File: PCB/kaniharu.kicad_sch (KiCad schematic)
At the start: 0 parts

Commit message: Remove autosave and lock files, add backup ZIP
Deleted KiCad autosave and lock files from the PCB directory and added a new backup ZIP file. Updated the main schematic file, likely reflecting recent design changes or cleanup.
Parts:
- added C10, C8, C9: C, symbol Device:C
- added C6, C7: 8p, symbol Device:C
- added J1: RJ45_Bel_SI-60062-F, Connector_RJ:RJ45_Bel_SI-60062-F, symbol Connector:RJ45_Bel_SI-60062-F
- added R5: 1.5k, symbol Device:R
- added R6, R7: 2.2k, symbol Device:R
- added R8: R, symbol Device:R
- added U1: STM32H743ZITx, Package_QFP:LQFP-144_20x20mm_P0.5mm, symbol MCU_ST_STM32H7:STM32H743ZITx
- added U3: DP83822IRHBR, DP83822IRHBR:IC_DP83822IRHBR, symbol 0_mylib:DP83822IRHBR
- added Y2: Crystal_GND24_Small, symbol Device:Crystal_GND24_Small
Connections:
- new net: C7.1, R8.1, Y2.3
- new net: U1.107 (VSS), U1.120 (VSS), U1.130 (VSS), U1.16 (VSS), U1.38 (VSS), U1.51 (VSS), U1.61 (VSS), U1.83 (VSS), U1.94 (VSS)
- new net: R6.2, U3.26 (RX_DV/RX_CTRL)
- new net: R8.2, U3.22 (XO)
- new net +3.3V: C10.1, C10.2, C6.2, C7.2, C8.1, C8.2, C9.1, C9.2, R5.1, R6.1, R7.1, U3.14 (AVD), U3.21 (VDDIO), Y2.2, Y2.4
- new net ETH_CRS_DV: R7.2, U1.43 (PA7), U3.27 (CRS/CRS_DV)
- new net ETH_MDC: U1.27 (PC1), U3.20 (MDC)
- new net ETH_MDIO: R5.2, U1.36 (PA2), U3.19 (MDIO)
- new net ETH_REF_CLK: C6.1, U1.35 (PA1), U3.23 (XI), Y2.1
- new net ETH_RXD0: U1.44 (PC4), U3.30 (RX_D0)
- new net ETH_RXD1: U1.45 (PC5), U3.31 (RX_D1)
- new net ETH_TXD0: U1.128 (PG13), U3.4 (TX_D0)
- new net ETH_TXD1: U1.127 (PG12), U3.5 (TX_D1)
- new net ETH_TX_EN: U1.126 (PG11), U3.3 (TX_EN/TX_CTRL)
- new net FDCAN1_RX: U1.114 (PD0)
- new net FDCAN1_TX: U1.115 (PD1)
- new net LPUART1_RX: U1.102 (PA10)
- new net LPUART_TX: U1.101 (PA9)
- new net SDMMC1_CK: U1.113 (PC12)
- new net SDMMC1_CMD: U1.116 (PD2)
- new net SDMMC1_D0: U1.98 (PC8)
- new net SDMMC1_D1: U1.99 (PC9)
- new net SDMMC1_D2: U1.111 (PC10)
- new net SDMMC1_D3: U1.112 (PC11)
- new net SWCLK: U1.109 (PA14)
- new net SWDIO: U1.105 (PA13)
- new net USB_OTG_FS_DM: U1.103 (PA11)
- new net USB_OTG_FS_DP: U1.104 (PA12)
- no-connect marks 0 -> 9

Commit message: update
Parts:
- removed C10, C8, C9: C, symbol Device:C
- removed C6, C7: 8p, symbol Device:C
- removed J1: RJ45_Bel_SI-60062-F, Connector_RJ:RJ45_Bel_SI-60062-F, symbol Connector:RJ45_Bel_SI-60062-F
- removed R5: 1.5k, symbol Device:R
- removed R6, R7: 2.2k, symbol Device:R
- removed R8: R, symbol Device:R
- removed U1: STM32H743ZITx, Package_QFP:LQFP-144_20x20mm_P0.5mm, symbol MCU_ST_STM32H7:STM32H743ZITx
- removed U3: DP83822IRHBR, DP83822IRHBR:IC_DP83822IRHBR, symbol 0_mylib:DP83822IRHBR
- removed Y2: Crystal_GND24_Small, symbol Device:Crystal_GND24_Small
- added C20, C21: C, Capacitor_SMD:C_0805_2012Metric_Pad1.18x1.45mm_HandSolder, symbol Device:C
- added C22: 10u, Capacitor_SMD:C_0805_2012Metric_Pad1.18x1.45mm_HandSolder, symbol Device:C
- added C23: 1u, Capacitor_SMD:C_0603_1608Metric_Pad1.08x0.95mm_HandSolder, symbol Device:C
- added D1, D2: D, 0_syslib:SODFL3618X110N, symbol Device:D
- added D3, D4: LED_ARBG, 0_syslib:OSTB0603C1CA, symbol Device:LED_ARBG
- added H1, H2, H3: MountingHole_Pad, MountingHole:MountingHole_3.2mm_M3, symbol Mechanical:MountingHole_Pad
- added H4: MountingHole_Pad, MountingHole:MountingHole_3.2mm_M3_Pad, symbol Mechanical:MountingHole_Pad
- added J2: USB_C_Receptacle_USB2.0_14P, Connector_USB:USB_C_Receptacle_HRO_TYPE-C-31-M-12, symbol Connector:USB_C_Receptacle_USB2.0_14P
- added J3, J4, J5: Conn_02x03_Odd_Even, Connector_IDC:IDC-Header_2x03_P2.54mm_Horizontal, symbol Connector_Generic:Conn_02x03_Odd_Even
- added JP1, JP2, JP3: Jumper_2_Open, Connector_PinHeader_2.54mm:PinHeader_1x02_P2.54mm_Vertical, symbol Jumper:Jumper_2_Open
- added L1: 22u, Inductor_SMD:L_0805_2012Metric_Pad1.15x1.40mm_HandSolder, symbol Device:L
- added PS1: RFM-0505S, 0_mylib:RFM-0505S, symbol 0_mylib:RFM-0505S
- added R10, R11, R12, R13, R14, R21, R22, R23, R9: R, Resistor_SMD:R_0402_1005Metric_Pad0.72x0.64mm_HandSolder, symbol Device:R
- added R15: 4.7k, Resistor_SMD:R_0603_1608Metric, symbol Device:R
- added R16: 4.7k, Resistor_SMD:R_0402_1005Metric_Pad0.72x0.64mm_HandSolder, symbol Device:R
- added U4: AZ1117-3.3, Package_TO_SOT_SMD:SOT-223-3_TabPin2, symbol Regulator_Linear:AZ1117-3.3
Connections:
- net +3.3V: now also C21.1, D3.1 (A), D4.1 (A), U4.2 (VO)
- new net: JP1.2 (B), R9.1
- new net: JP2.2 (B), R10.1
- new net: D4.2 (RK), R23.2
- new net: D4.3 (BK), R21.2
- new net: D4.4 (GK), R22.2
- new net: C23.1, D1.2 (A), PS1.4 (+VOUT)
- new net: D3.2 (RK), R14.2
- new net: D3.3 (BK), R12.2
- new net: D3.4 (GK), R13.2
- new net: D2.1 (K), J2.A4 (VBUS), J2.A9 (VBUS), J2.B4 (VBUS), J2.B9 (VBUS)
- new net: J2.A5 (CC1), R15.2
- new net: J2.B5 (CC2), R16.2
- new net: L1.2, PS1.2 (+VIN)
- new net: JP3.2 (B), R11.1
- new net +5V: C20.1, C22.1, D2.2 (A), L1.1, U4.3 (VI)
- new net +5VA: D1.1 (K), J3.1 (Pin_1), J4.1 (Pin_1), J5.1 (Pin_1)
- new net CAN1/CAN1H: J3.3 (Pin_3), R9.2
- new net CAN1/CAN1L: J3.4 (Pin_4), JP1.1 (A)
- new net CAN2/CAN2H: J4.3 (Pin_3), R10.2
- new net CAN2/CAN2L: J4.4 (Pin_4), JP2.1 (A)
- new net CAN3/CAN3H: J5.3 (Pin_3), R11.2
- new net CAN3/CAN3L: J5.4 (Pin_4), JP3.1 (A)
- new net GND: C20.2, C21.2, C22.2, H4.1, J2.A1 (GND), J2.A12 (GND), J2.B1 (GND), J2.B12 (GND), PS1.1 (-VIN), R15.1, R16.1, U4.1 (GND)
- new net GNDPWR: C23.2, J3.6 (Pin_6), J4.6 (Pin_6), J5.6 (Pin_6), PS1.3 (-VOUT)
- new net MCU/TIM1_CH1: R12.1
- new net MCU/TIM1_CH2: R14.1
- new net MCU/TIM1_CH3: R13.1
- new net MCU/TIM3_CH1: R21.1
- new net MCU/TIM3_CH2: R22.1
- new net MCU/TIM3_CH3: R23.1
- new net MCU/USB_OTG_FS_DM: J2.A7 (D-), J2.B7 (D-)
- new net MCU/USB_OTG_FS_DP: J2.A6 (D+), J2.B6 (D+)
- no-connect marks 9 -> 10
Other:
- added sheet CAN1 (CAN1.kicad_sch)
- added sheet CAN2 (CAN2.kicad_sch)
- added sheet CAN3 (CAN3.kicad_sch)
- added sheet ETH (ETH.kicad_sch)
- added sheet MCU (untitled.kicad_sch)

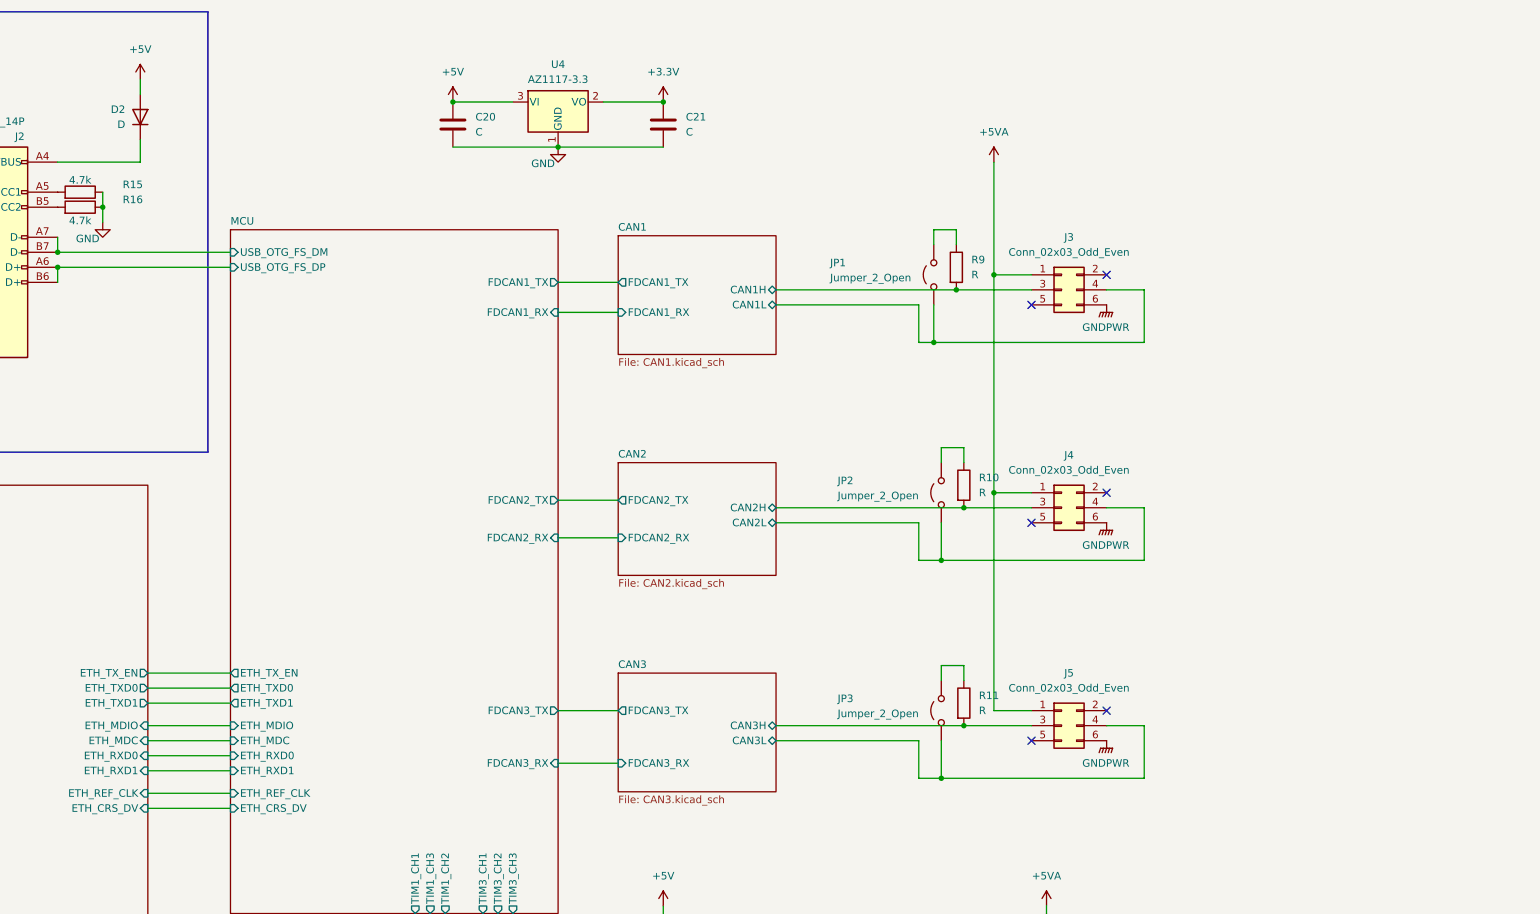
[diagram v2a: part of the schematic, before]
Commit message: 電源以外配線おわり
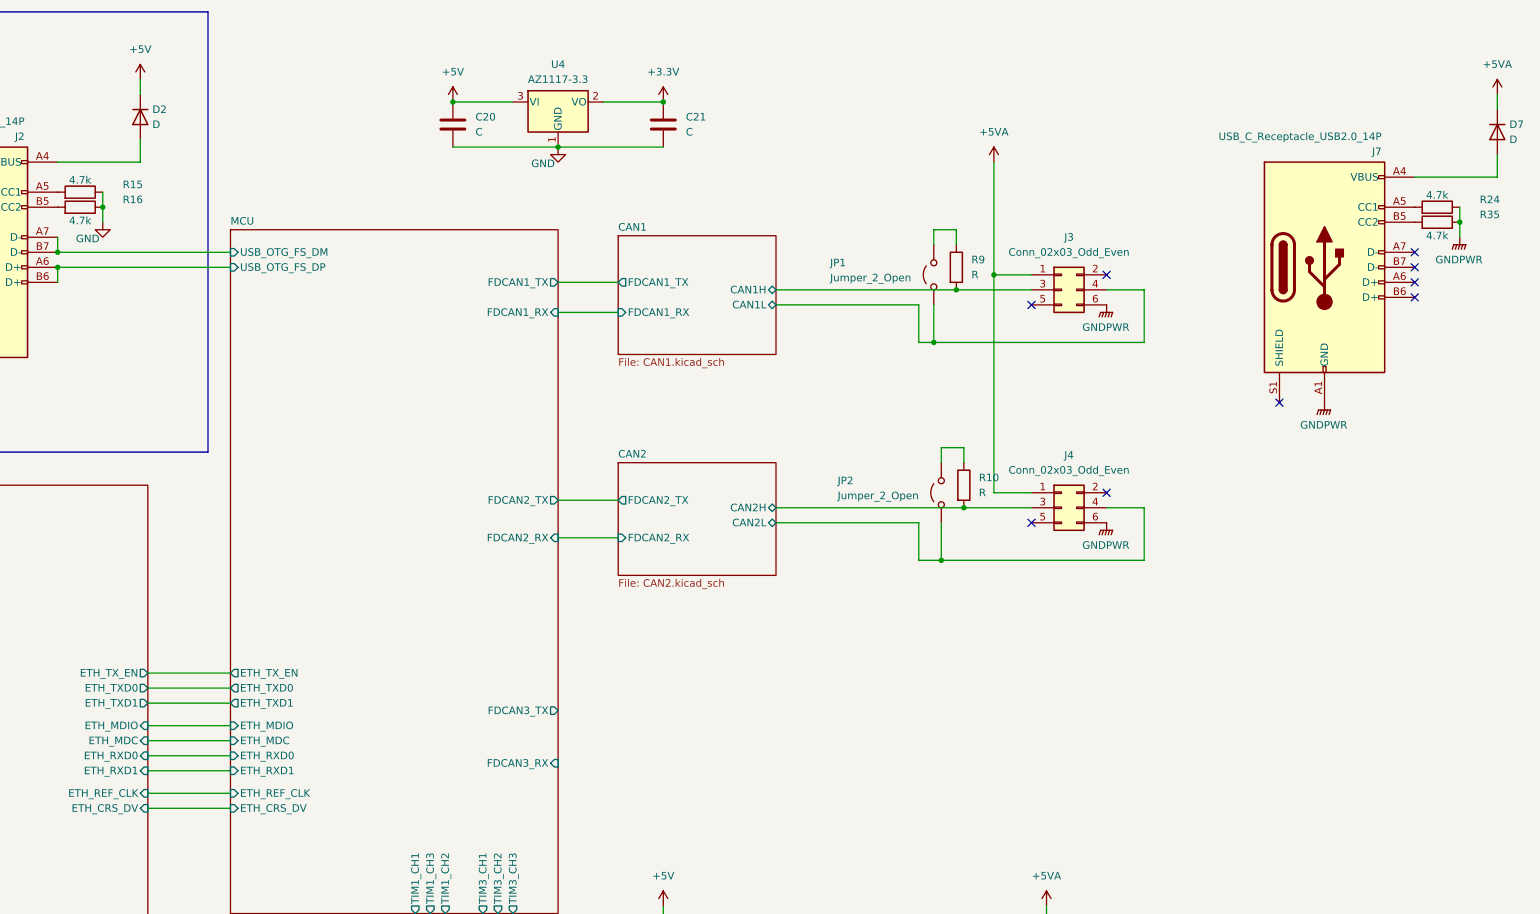
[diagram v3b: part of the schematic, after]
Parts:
- removed J5: Conn_02x03_Odd_Even, Connector_IDC:IDC-Header_2x03_P2.54mm_Horizontal, symbol Connector_Generic:Conn_02x03_Odd_Even
- removed JP3: Jumper_2_Open, Connector_PinHeader_2.54mm:PinHeader_1x02_P2.54mm_Vertical, symbol Jumper:Jumper_2_Open
- removed R11: R, Resistor_SMD:R_0402_1005Metric_Pad0.72x0.64mm_HandSolder, symbol Device:R
- added D7: D, 0_syslib:SODFL3618X110N, symbol Device:D
- added J7: USB_C_Receptacle_USB2.0_14P, Connector_USB:USB_C_Receptacle_HRO_TYPE-C-31-M-12, symbol Connector:USB_C_Receptacle_USB2.0_14P
- added R24, R35: 4.7k, Resistor_SMD:R_0603_1608Metric_Pad0.98x0.95mm_HandSolder, symbol Device:R
- R10, R12, R13, R14, R16, R21, R22, R23, R9: footprint Resistor_SMD:R_0402_1005Metric_Pad0.72x0.64mm_HandSolder -> Resistor_SMD:R_0603_1608Metric_Pad0.98x0.95mm_HandSolder
- R15: footprint Resistor_SMD:R_0603_1608Metric -> Resistor_SMD:R_0603_1608Metric_Pad0.98x0.95mm_HandSolder
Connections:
- net +5V: now also D2.1 (K); no longer D2.2 (A)
- net +5VA: now also D7.1 (K)
- net GNDPWR: now also J7.A1 (GND), J7.A12 (GND), J7.B1 (GND), J7.B12 (GND), R24.1, R35.1
- net at J2.A4 (VBUS), J2.A9 (VBUS), J2.B4 (VBUS)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: now also D2.2 (A); no longer D2.1 (K)
- new net: D7.2 (A), J7.A4 (VBUS), J7.A9 (VBUS), J7.B4 (VBUS), J7.B9 (VBUS)
- new net: J7.A5 (CC1), R24.2
- new net: J7.B5 (CC2), R35.2
- no-connect marks 10 -> 13
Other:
- removed sheet CAN3
- moved on the sheet: D2

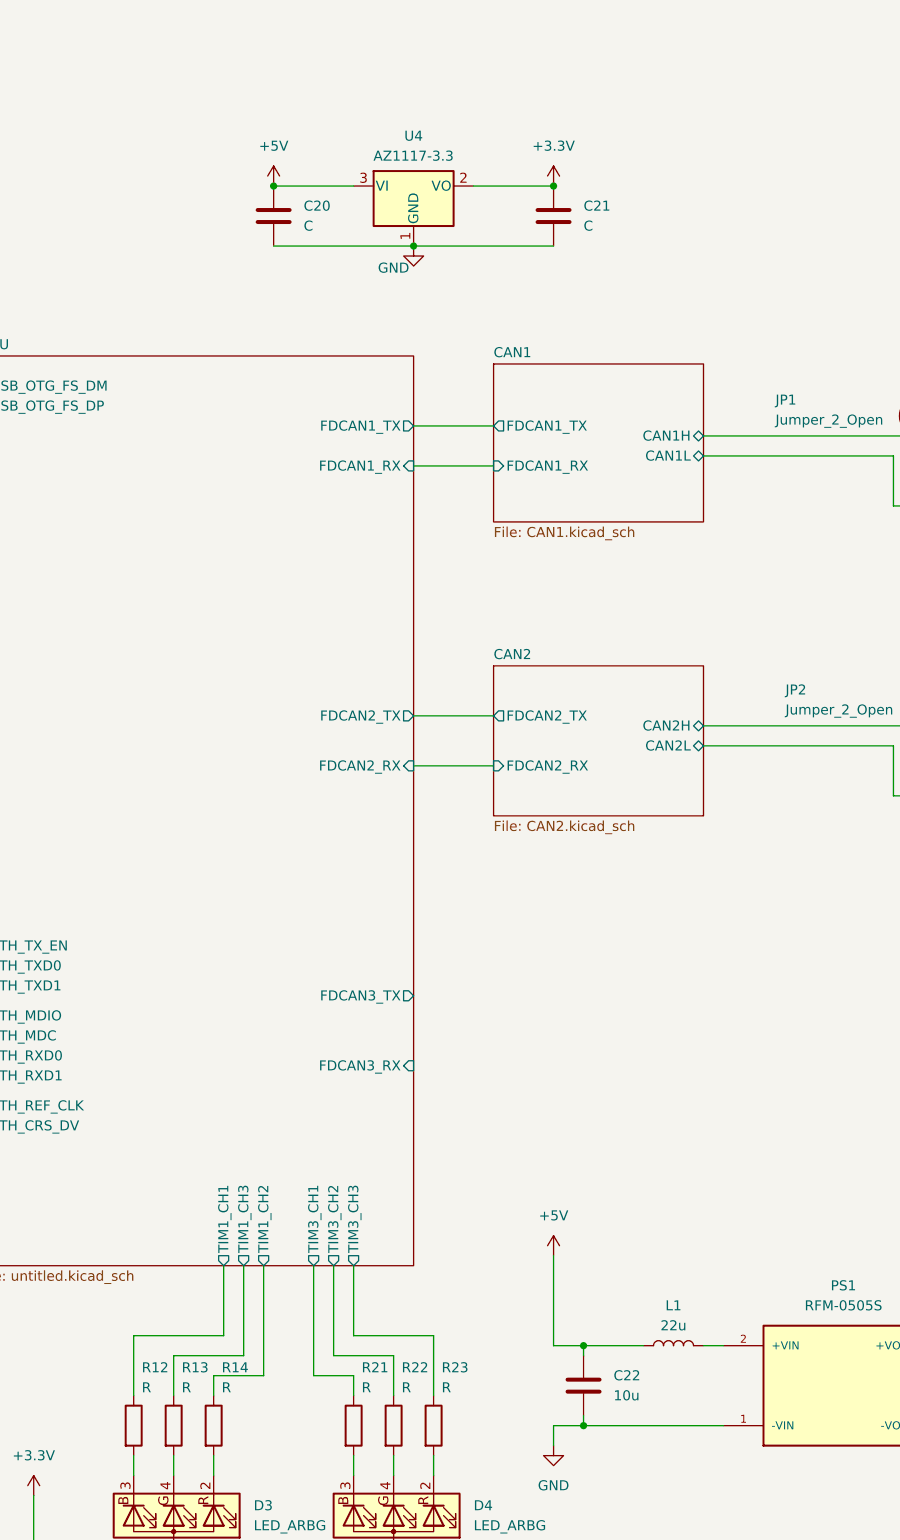
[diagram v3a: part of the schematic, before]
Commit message: update:基板発注した
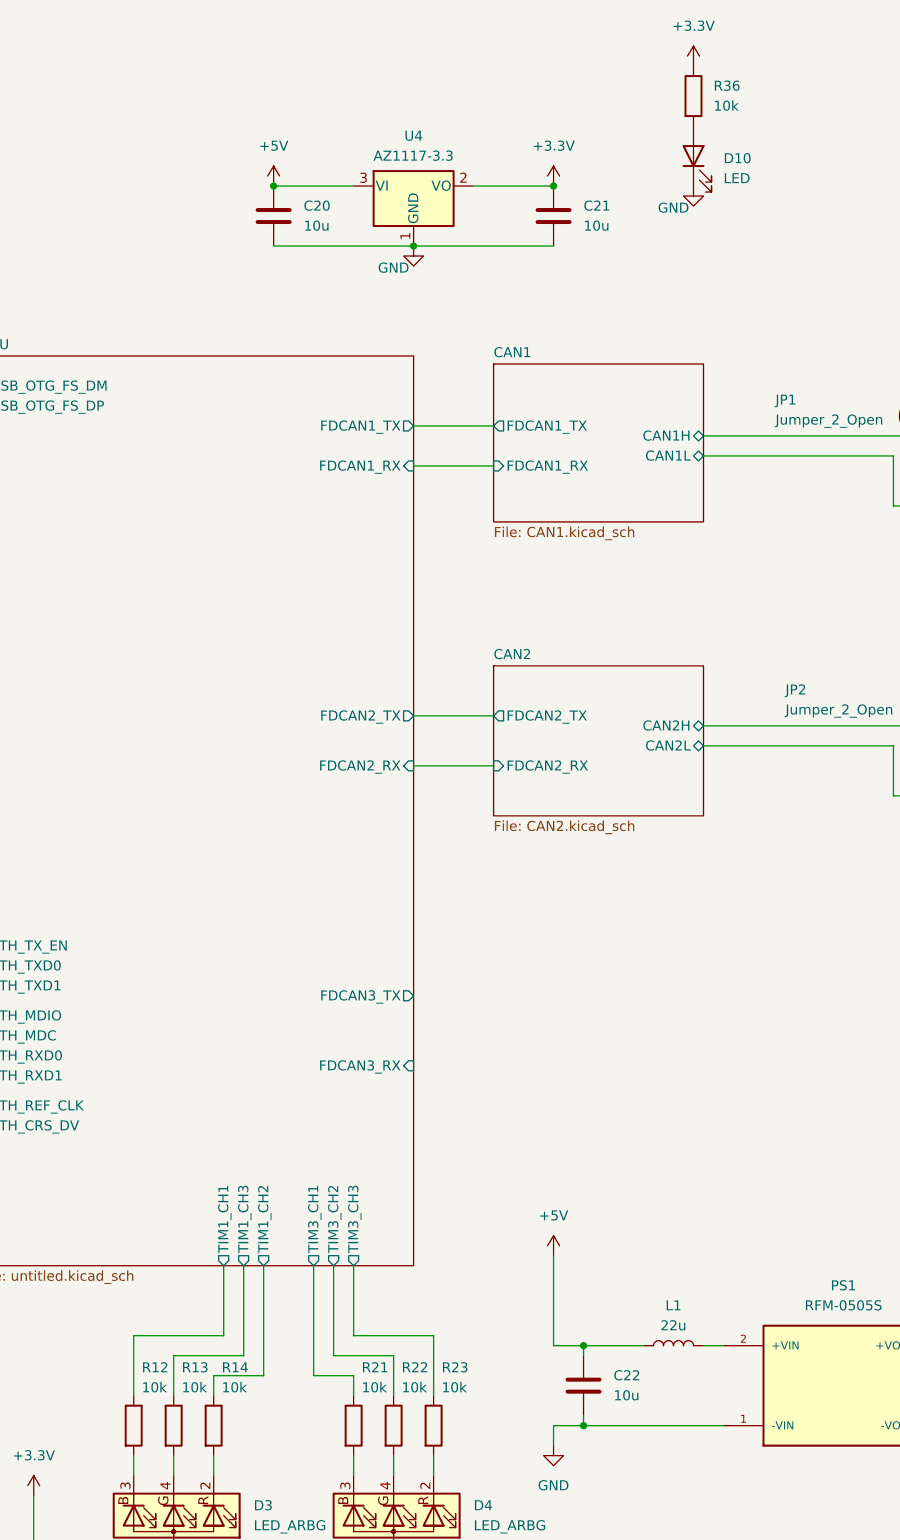
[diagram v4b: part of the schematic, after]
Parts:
- added D10: LED, LED_SMD:LED_0603_1608Metric_Pad1.05x0.95mm_HandSolder, symbol Device:LED
- added R36: 10k, Resistor_SMD:R_0603_1608Metric_Pad0.98x0.95mm_HandSolder, symbol Device:R
- C20, C21: value C -> 10u
- R12, R13, R14, R21, R22, R23: value R -> 10k
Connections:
- net +3.3V: now also R36.1
- net GND: now also D10.1 (K)
- new net: D10.2 (A), R36.2
